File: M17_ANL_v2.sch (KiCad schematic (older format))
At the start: 101 parts, among them IC1 ADF7021, J1 USB_A, J2 RF_PORT, J3 Conn_01x05, U1 STM32F303CBTx, U2 AP1117-33, X1 ASV-xxxMHz, X2 ASV-xxxMHz

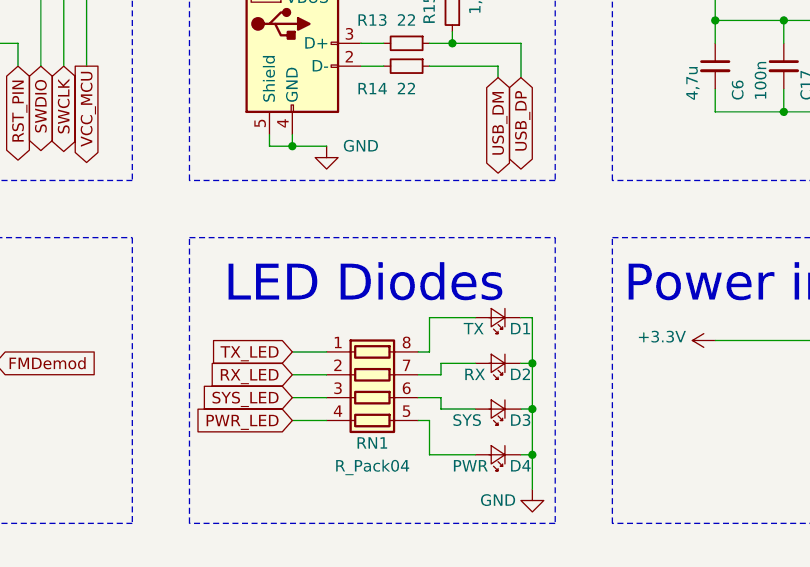
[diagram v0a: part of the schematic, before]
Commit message: Diodes description changed
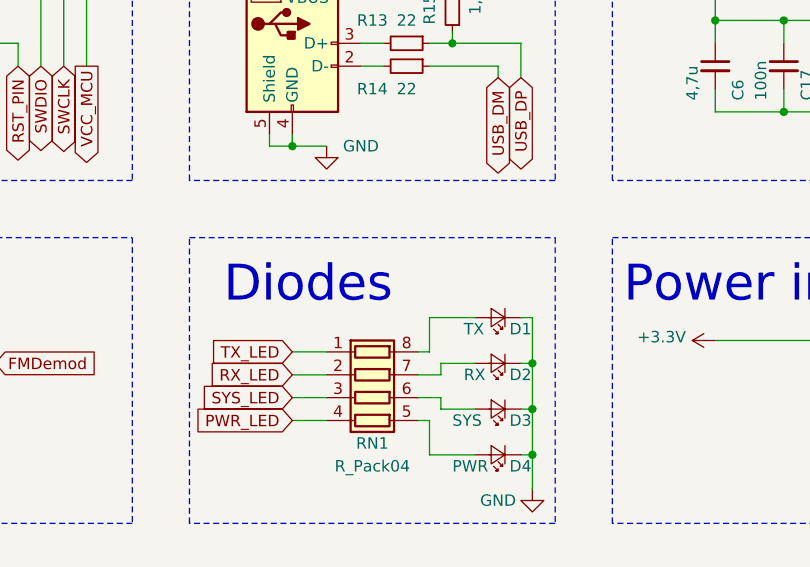
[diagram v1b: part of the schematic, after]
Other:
- note added: "Diodes"
- note removed: "LED Diodes"
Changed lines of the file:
@@
 	4500 6850 6100 6850
 Text Notes 4650 7150 0    157  ~ 0
-LED Diodes
+Diodes
 Text GLabel 4950 7650 0    50   Input ~ 0
 PWR_LED

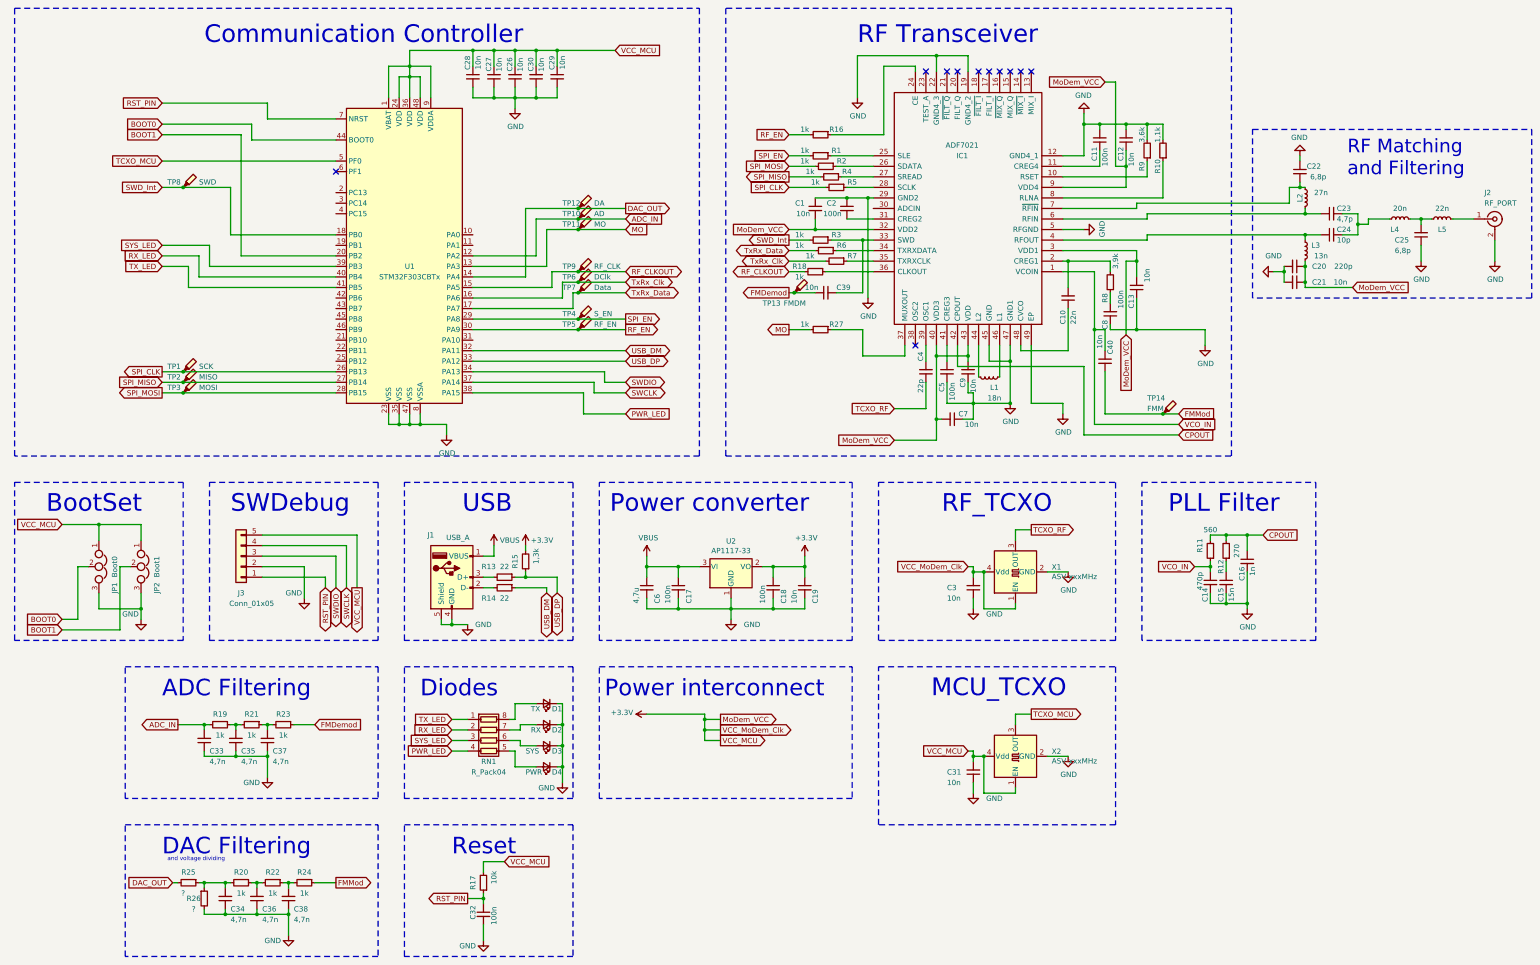
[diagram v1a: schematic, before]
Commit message: Added header to unused pins of STM32
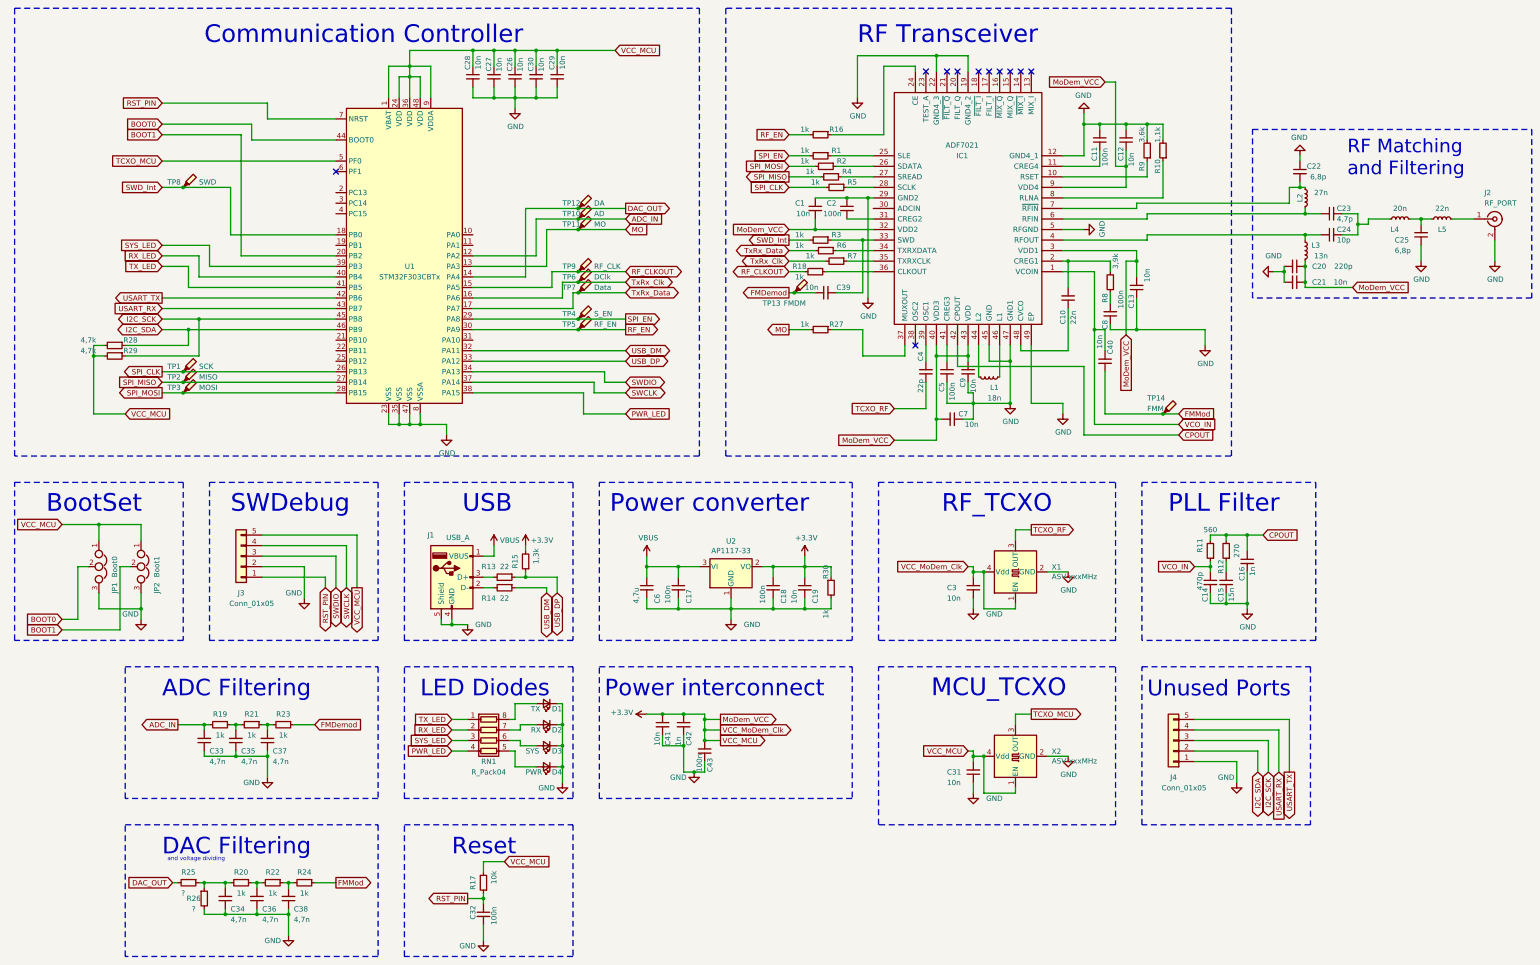
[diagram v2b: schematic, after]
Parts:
- added C41: 10n, Capacitor_SMD:C_0805_2012Metric, symbol Device:C_Small
- added C42: 1n, Capacitor_SMD:C_0805_2012Metric, symbol Device:C_Small
- added C43: 100n, Capacitor_SMD:C_0805_2012Metric, symbol Device:C_Small
- added J4: Conn_01x05, Connector_PinHeader_1.27mm:PinHeader_1x05_P1.27mm_Vertical, symbol Connector_Generic:Conn_01x05
- added R28, R29: 4,7k, Resistor_SMD:R_0402_1005Metric, symbol Device:R_Small
- added R30: 1k, Resistor_SMD:R_0805_2012Metric, symbol Device:R_Small
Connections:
- net +3V3: now also C41.1, C42.1, C43.1, R28.2, R29.2, R30.1
- net GND: now also C41.2, C42.2, C43.2, J4.1 (Pin_1), R30.2
- net USART_TX: now reaches U1.42 (PB6)
- net USART_TX: now also J4.5 (Pin_5)
- net USART_RX: now reaches U1.43 (PB7)
- net USART_RX: now also J4.4 (Pin_4)
- net I2C_SCK: now reaches U1.45 (PB8)
- net I2C_SCK: now also J4.3 (Pin_3), R29.1
- net I2C_SDA: now reaches U1.46 (PB9)
- net I2C_SDA: now also J4.2 (Pin_2), R28.1
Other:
- note added: "LED Diodes"
- note added: "Unused Ports\n"
- note removed: "Diodes"
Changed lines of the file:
@@
 Sheet 1 1
 Title "M17_ANL"
-Date "2019-12-29"
+Date ""
 Rev "v2"
-Comp "Nikoloz Glonti / NG91 / SO3ALG"
+Comp "Nikoloz Glonti"
 Comment1 "SiModeM v2"
 Comment2 "DRAFT! Not released Yet"
@@
 VCC_MoDem_Clk
 Wire Wire Line
-	6800 7300 7350 7300
+	6800 7300 6950 7300
 Wire Wire Line
 	7350 7300 7350 7350
@@
 	4500 6850 6100 6850
 Text Notes 4650 7150 0    157  ~ 0
-Diodes
+LED Diodes
 Text GLabel 4950 7650 0    50   Input ~ 0
 PWR_LED
@@
 Wire Wire Line
 	6150 2500 5650 2500
+Wire Notes Line width 10 style solid
+	13100 6850 13100 8350
+Wire Notes Line width 10 style solid
+	13100 8350 11500 8350
+Wire Notes Line width 10 style solid
+	11500 8350 11500 6850
+Wire Notes Line width 10 style solid
+	11500 6850 13100 6850
+Text Notes 11550 7150 0    150  ~ 0
+Unused Ports\n
+Text GLabel 12700 7850 3    50   BiDi ~ 0
+I2C_SCK
+Text GLabel 12800 7850 3    50   Input ~ 0
+USART_RX
+$Comp
+L Connector_Generic:Conn_01x05 J4
+U 1 1 5E2C21E2
+P 11800 7550
+F 0 "J4" H 11800 7900 50  0000 C CNN
+F 1 "Conn_01x05" H 11700 8000 50  0000 C CNN
+F 2 "Connector_PinHeader_1.27mm:PinHeader_1x05_P1.27mm_Vertical" H 11800 7550 50  0001 C CNN
+F 3 "~" H 11800 7550 50  0001 C CNN
+	1    11800 7550
+	-1   0    0    1
+$EndComp
+Text GLabel 12600 7850 3    50   BiDi ~ 0
+I2C_SDA
+Wire Wire Line
+	12000 7550 12700 7550
+Wire Wire Line
+	12700 7550 12700 7850
+Wire Wire Line
+	12800 7850 12800 7450
+Wire Wire Line
+	12800 7450 12000 7450
+Text GLabel 12900 7850 3    50   Output ~ 0
+USART_TX
+Wire Wire Line
+	12900 7850 12900 7350
+Wire Wire Line
+	12900 7350 12000 7350
+$Comp
+L power:GND #PWR0107
+U 1 1 5E2C21F2
+P 12400 7950
+F 0 "#PWR0107" H 12400 7700 50  0001 C CNN
+F 1 "GND" H 12300 8000 50  0000 C CNN
+F 2 "" H 12400 7950 50  0001 C CNN
+F 3 "" H 12400 7950 50  0001 C CNN
+	1    12400 7950
+	1    0    0    -1
+$EndComp
+Wire Wire Line
+	12000 7750 12400 7750
+Wire Wire Line
+	12400 7750 12400 7950
+Wire Wire Line
+	12600 7650 12000 7650
+Wire Wire Line
+	12600 7650 12600 7850
+Text GLabel 2200 3350 0    50   Output ~ 0
+USART_TX
+Text GLabel 2200 3450 0    50   Input ~ 0
+USART_RX
+Wire Wire Line
+	3850 3350 2200 3350
+Wire Wire Line
+	2200 3450 3850 3450
+Text GLabel 2200 3550 0    50   BiDi ~ 0
+I2C_SCK
+Text GLabel 2200 3650 0    50   BiDi ~ 0
+I2C_SDA
+Wire Wire Line
+	2200 3650 2450 3650
+$Comp
+L Device:R_Small R28
+U 1 1 5E633874
+P 1750 3800
+F 0 "R28" V 1700 3950 50  0000 C CNN
+F 1 "4,7k" V 1700 3550 50  0000 C CNN
+F 2 "Resistor_SMD:R_0402_1005Metric" H 1750 3800 50  0001 C CNN
+F 3 "~" H 1750 3800 50  0001 C CNN
+	1    1750 3800
+	0    1    1    0
+$EndComp
+Text GLabel 1850 4450 2    50   Input ~ 0
+VCC_MCU
+Wire Wire Line
+	1850 4450 1550 4450
+Wire Wire Line
+	1550 4450 1550 3900
+Wire Wire Line
+	1550 3800 1650 3800
+Wire Wire Line
+	1650 3900 1550 3900
+Connection ~ 1550 3900
+Wire Wire Line
+	1550 3900 1550 3800
+Wire Wire Line
+	1850 3900 2550 3900
+Wire Wire Line
+	2550 3900 2550 3550
+Connection ~ 2550 3550
+Wire Wire Line
+	2550 3550 3850 3550
+Wire Wire Line
+	2200 3550 2550 3550
+Wire Wire Line
+	2450 3650 2450 3800
+Wire Wire Line
+	2450 3800 1850 3800
+Connection ~ 2450 3650
+$Comp
+L Device:R_Small R29
+U 1 1 5E62CDA3
+P 1750 3900
+F 0 "R29" V 1700 4050 50  0000 C CNN
+F 1 "4,7k" V 1700 3650 50  0000 C CNN
+F 2 "Resistor_SMD:R_0402_1005Metric" H 1750 3900 50  0001 C CNN
+F 3 "~" H 1750 3900 50  0001 C CNN
+	1    1750 3900
+	0    1    1    0
+$EndComp
+Wire Wire Line
+	2450 3650 3850 3650
+$Comp
+L Device:R_Small R30
+U 1 1 5E2C095C
+P 8550 6100
+F 0 "R30" V 8500 6250 50  0000 C CNN
+F 1 "1k" V 8500 5850 50  0000 C CNN
+F 2 "Resistor_SMD:R_0805_2012Metric" H 8550 6100 50  0001 C CNN
+F 3 "~" H 8550 6100 50  0001 C CNN
+	1    8550 6100
+	1    0    0    -1
+$EndComp
+Wire Wire Line
+	8300 5900 8550 5900
+Wire Wire Line
+	8550 5900 8550 6000
+Wire Wire Line
+	8550 6200 8550 6300
+Wire Wire Line
+	8550 6300 8300 6300
+Connection ~ 8300 6300
+$Comp
+L Device:C_Small C41
+U 1 1 5E354E9A
+P 6950 7400
+F 0 "C41" V 7000 7200 50  0000 L CNN
+F 1 "10n" V 6900 7200 50  0000 L CNN
+F 2 "Capacitor_SMD:C_0805_2012Metric" H 6950 7400 50  0001 C CNN
+F 3 "~" H 6950 7400 50  0001 C CNN
+	1    6950 7400
+	1    0    0    -1
+$EndComp
+Connection ~ 6950 7300
+Wire Wire Line
+	6950 7300 7150 7300
+$Comp
+L Device:C_Small C42
+U 1 1 5E356886
+P 7150 7400
+F 0 "C42" V 7200 7200 50  0000 L CNN
+F 1 "1n" V 7100 7200 50  0000 L CNN
+F 2 "Capacitor_SMD:C_0805_2012Metric" H 7150 7400 50  0001 C CNN
+F 3 "~" H 7150 7400 50  0001 C CNN
+	1    7150 7400
+	1    0    0    -1
+$EndComp
+Connection ~ 7150 7300
+Wire Wire Line
+	7150 7300 7350 7300
+$Comp
+L Device:C_Small C43
+U 1 1 5E356D2D
+P 7350 7650
+F 0 "C43" V 7400 7450 50  0000 L CNN
+F 1 "100n" V 7300 7450 50  0000 L CNN
+F 2 "Capacitor_SMD:C_0805_2012Metric" H 7350 7650 50  0001 C CNN
+F 3 "~" H 7350 7650 50  0001 C CNN
+	1    7350 7650
+	1    0    0    -1
+$EndComp
+Connection ~ 7350 7550
+Wire Wire Line
+	6950 7500 6950 7600
+Wire Wire Line
+	6950 7600 7150 7600
+Wire Wire Line
+	7150 7600 7150 7500
+Wire Wire Line
+	7150 7600 7150 7850
+Wire Wire Line
+	7150 7850 7250 7850
+Wire Wire Line
+	7350 7850 7350 7750
+Connection ~ 7150 7600
+$Comp
+L power:GND #PWR0108
+U 1 1 5E3EC904
+P 7250 7850
+F 0 "#PWR0108" H 7250 7600 50  0001 C CNN
+F 1 "GND" H 7100 7800 50  0000 C CNN
+F 2 "" H 7250 7850 50  0001 C CNN
+F 3 "" H 7250 7850 50  0001 C CNN
+	1    7250 7850
+	1    0    0    -1
+$EndComp
+Connection ~ 7250 7850
+Wire Wire Line
+	7250 7850 7350 7850
 $EndSCHEMATC
